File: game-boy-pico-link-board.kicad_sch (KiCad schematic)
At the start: 6 parts, among them J1 GBA_Link, J2 GB_Link, J3 Breakout, SW1 SW_SPDT, U1 Pico, U2 BOB-12009

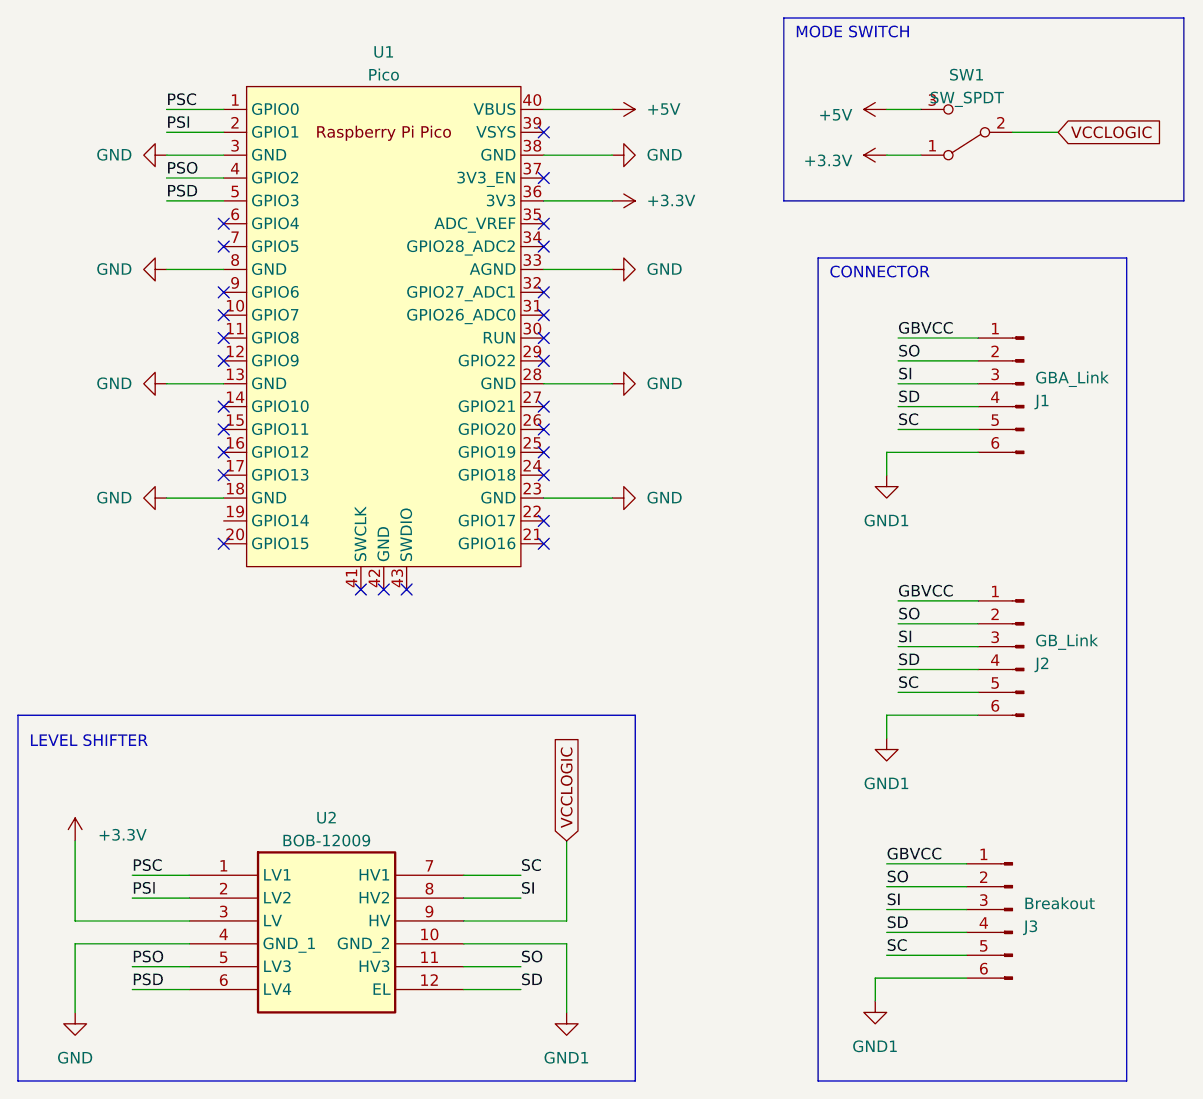
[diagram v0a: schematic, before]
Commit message: Update Design and Add Routing
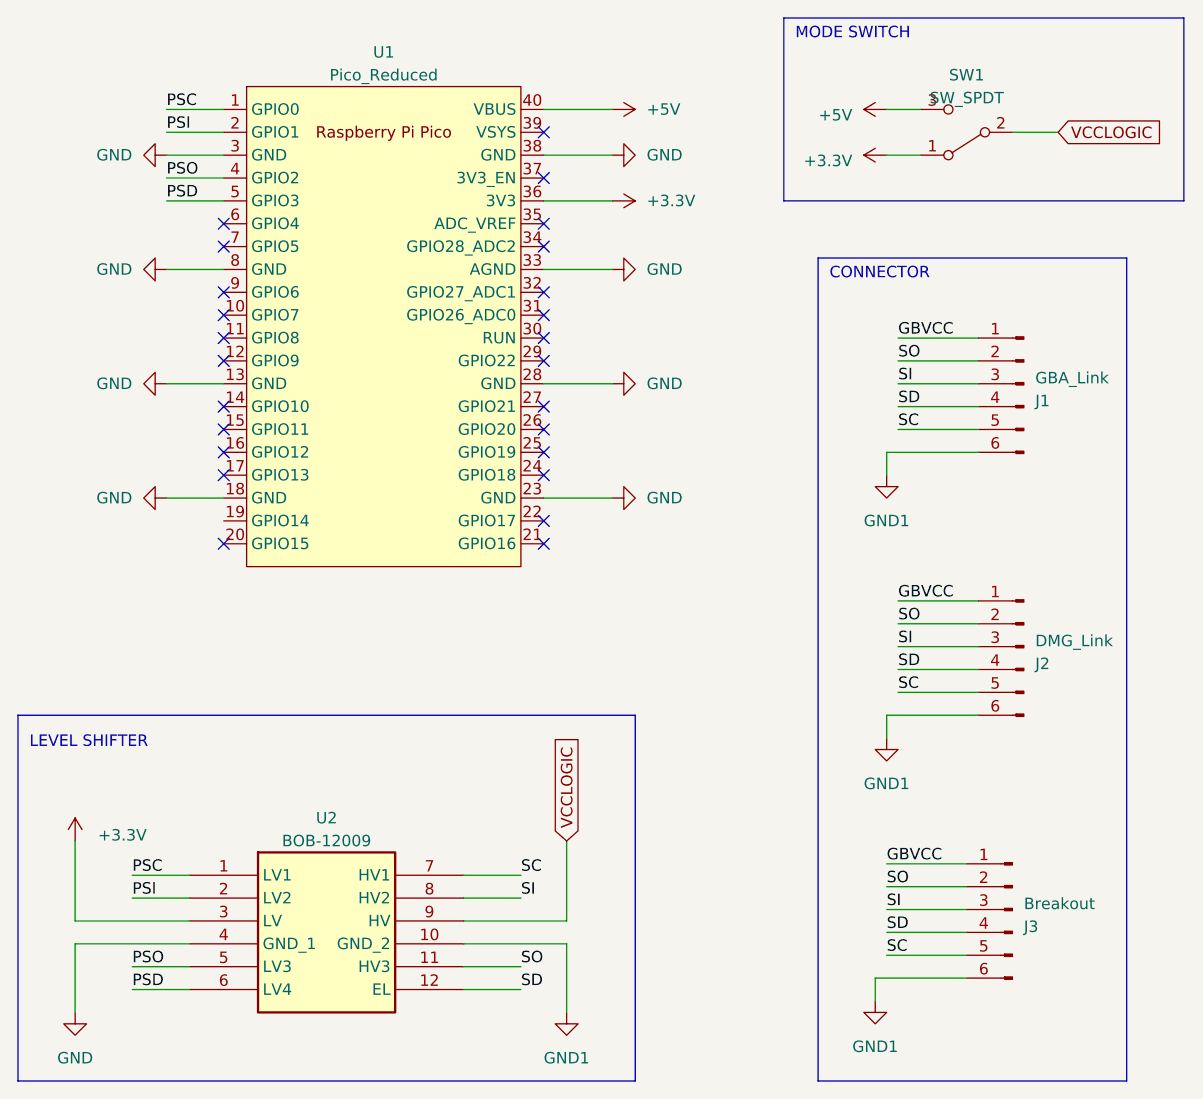
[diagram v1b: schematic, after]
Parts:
- removed U1: Pico, MCU_RaspberryPi_and_Boards:RPi_Pico_SMD_TH, symbol MCU_RaspberryPi_and_Boards:Pico
- added U1: Pico_Reduced, MCU_RaspberryPi_and_Boards:RPi_Pico_SMD_TH_REDUCED, symbol MCU_RaspberryPi_and_Boards:Pico_Reduced
- J2: value GB_Link -> DMG_Link; footprint gb-link-socket:gb-link-socket -> gb-link-socket:dmg-link-socket
- SW1: footprint Connector_PinHeader_2.54mm:PinHeader_1x03_P2.54mm_Horizontal -> Connector_PinHeader_2.54mm:PinHeader_1x03_P2.54mm_Vertical
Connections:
- net +3.3V: now also U1.36 (3V3)
- net +5V: now also U1.40 (VBUS)
- net GND: now also U1.13 (GND), U1.18 (GND), U1.23 (GND), U1.28 (GND), U1.3 (GND), U1.33 (AGND), U1.38 (GND), U1.8 (GND)
- net PSC: now also U1.1 (GPIO0)
- net PSD: now also U1.5 (GPIO3)
- net PSI: now also U1.2 (GPIO1)
- net PSO: now also U1.4 (GPIO2)
- no-connect marks 28 -> 25
